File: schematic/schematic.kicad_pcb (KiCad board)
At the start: 4 copper layers, 100 x 100 mm, 260 parts, among them J1 Conn_01x04, J10 Conn_01x03, J11 Conn_01x02, J12 Conn_01x02, J13 Conn_01x02, J14 Conn_01x02, J15 Conn_01x02, J16 Conn_01x02, J17 Conn_01x04, J18 Conn_02x13_Odd_Even, J2 Conn_01x04, J3 Conn_01x04, J4 Conn_01x04, J5 Conn_01x04, J6 Conn_01x06, J7 Conn_01x03, J8 Screw_Terminal_01x02, J9 Conn_01x03, Q1 PSMN1R7-30YL, Q2 PSMN1R7-30YL, Q3 NCV8402, Q4 NCV8402, SW1 SW_Push_Dual, SW2 SW_DIP_x03, U1 STM32F401VETx, U2 TMC2130, U3 TMC2130, U4 TMC2130, U5 TMC2130, U6 BD9E302EFJ, U7 BD9E302EFJ, U8 BD9E302EFJ, Y1 Crystal_GND24

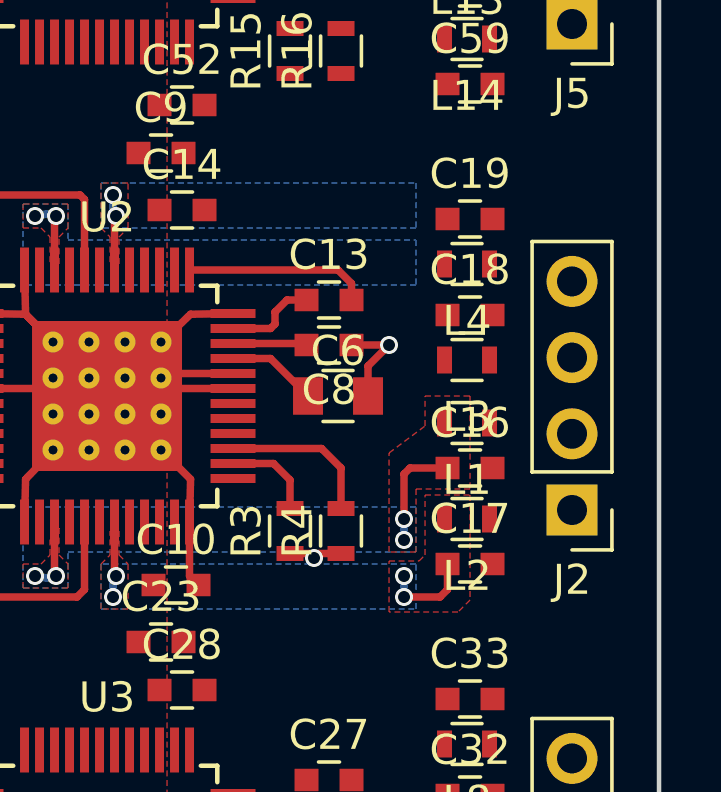
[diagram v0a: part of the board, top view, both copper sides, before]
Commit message: Power layout single driver done
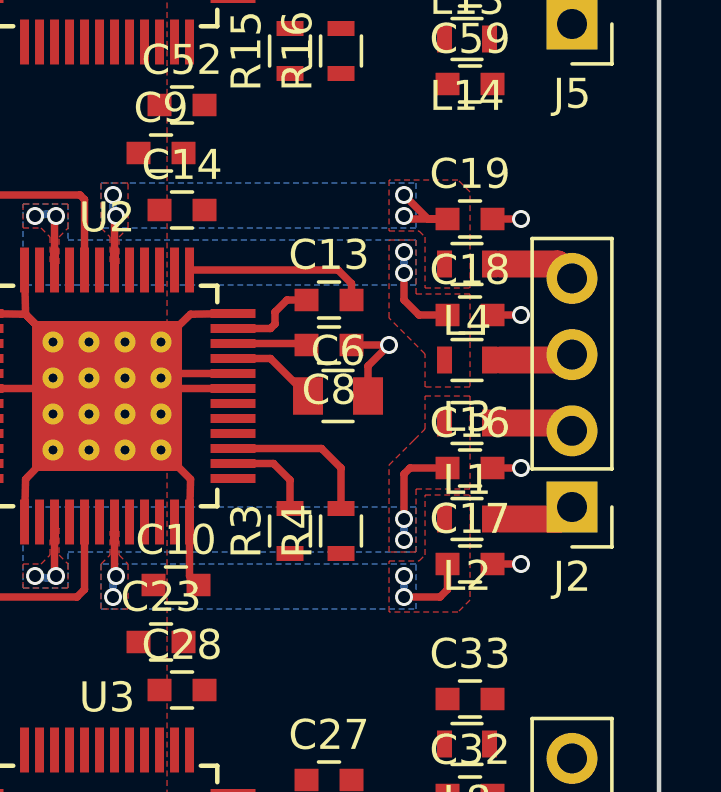
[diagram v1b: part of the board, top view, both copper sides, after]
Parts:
- moved J2 0.10 mm to (262.1, 110.9)
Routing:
- net GND: track 214.8 -> 218.6 mm, vias 78 -> 82
- net Net-(C19-Pad1): track 2.56 -> 5.83 mm, vias 2 -> 4
- net Net-(C18-Pad1): track 2.57 -> 5.83 mm, vias 2 -> 4
- net /MotorX/B2: track 0.00 -> 2.95 mm
- net /MotorX/B1: track 0.00 -> 2.92 mm
- net /MotorX/A1: track 0.00 -> 2.86 mm
- net /MotorX/A2: track 0.00 -> 2.82 mm
- net +3V3: track 3.84 -> 2.01 mm, vias 1 -> 0
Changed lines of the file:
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@@
   (general
     (links 833)
-    (no_connects 352)
+    (no_connects 341)
     (area 133.3 48.325 267.04762 154.782382)
     (thickness 1.6)
     (drawings 4)
-    (tracks 511)
+    (tracks 538)
     (zones 0)
     (modules 260)
@@
     (last_trace_width 0.25)
     (user_trace_width 0.7)
+    (user_trace_width 0.9)
     (user_trace_width 1.5)
     (user_trace_width 2.2)
@@
   )
   (module Socket_Strips:Socket_Strip_Straight_1x04_Pitch2.54mm (layer F.Cu)
-    (at 262.1 111 180)
+    (at 262.1 110.9 180)
     (descr "Through hole straight socket strip, 1x04, 2.54mm pitch, single row")
     (tags "Through hole socket strip THT 1x04 2.54mm single row")
@@
   (gr_line (start 265 50) (end 165 50) (angle 90) (layer Edge.Cuts) (width 0.15))
   (gr_line (start 265 150) (end 265 50) (angle 90) (layer Edge.Cuts) (width 0.15))
+  (segment (start 259.45 101.3) (end 260.4 101.3) (width 0.25) (layer F.Cu) (net 1))
+  (via (at 260.4 101.3) (size 0.6) (drill 0.4) (layers F.Cu B.Cu) (net 1))
+  (segment (start 259.45 104.5) (end 260.4 104.5) (width 0.25) (layer F.Cu) (net 1))
+  (via (at 260.4 104.5) (size 0.6) (drill 0.4) (layers F.Cu B.Cu) (net 1))
+  (segment (start 259.45 112.8) (end 260.4 112.8) (width 0.25) (layer F.Cu) (net 1))
+  (via (at 260.4 112.8) (size 0.6) (drill 0.4) (layers F.Cu B.Cu) (net 1))
+  (segment (start 259.45 109.6) (end 260.4 109.6) (width 0.25) (layer F.Cu) (net 1))
+  (via (at 260.4 109.6) (size 0.6) (drill 0.4) (layers F.Cu B.Cu) (net 1))
   (segment (start 227.3 141.35) (end 227.3 140.6) (width 0.25) (layer B.Cu) (net 1))
   (segment (start 227.3 140.6) (end 228 139.9) (width 0.25) (layer B.Cu) (net 1))
@@
   (segment (start 250.8 105.95) (end 252.05 105.95) (width 0.25) (layer F.Cu) (net 7) (status 10))
   (segment (start 252.05 105.95) (end 253.3 107.2) (width 0.25) (layer F.Cu) (net 7))
-  (segment (start 252.7 112.45) (end 253.35 112.45) (width 0.25) (layer F.Cu) (net 8))
-  (segment (start 253.65 112.45) (end 253.5 112.6) (width 0.25) (layer F.Cu) (net 8))
-  (via (at 253.5 112.6) (size 0.6) (drill 0.4) (layers F.Cu B.Cu) (net 8))
-  (segment (start 253.65 112.45) (end 254.4 112.45) (width 0.25) (layer F.Cu) (net 8))
-  (segment (start 253.35 112.45) (end 253.5 112.6) (width 0.25) (layer F.Cu) (net 8))
   (segment (start 242.4 108.95) (end 240.6 108.95) (width 0.25) (layer F.Cu) (net 8) (status 10))
   (segment (start 240.6 108.95) (end 240.45 109.1) (width 0.25) (layer F.Cu) (net 8))
@@
   (via (at 246.9 113.2) (size 0.6) (drill 0.4) (layers F.Cu B.Cu) (net 16))
   (segment (start 246.85 113.15) (end 246.9 113.2) (width 0.25) (layer F.Cu) (net 16))
+  (segment (start 256.5 102.4) (end 256.5 103.1) (width 0.25) (layer B.Cu) (net 17))
+  (segment (start 257 104.5) (end 256.5 104) (width 0.25) (layer F.Cu) (net 17))
+  (segment (start 256.5 104) (end 256.5 103.1) (width 0.25) (layer F.Cu) (net 17))
+  (via (at 256.5 103.1) (size 0.6) (drill 0.4) (layers F.Cu B.Cu) (net 17))
+  (segment (start 257 104.5) (end 257.95 104.5) (width 0.25) (layer F.Cu) (net 17))
+  (via (at 256.5 102.4) (size 0.6) (drill 0.4) (layers F.Cu B.Cu) (net 17))
   (segment (start 244.85 103) (end 244.85 101.25) (width 0.25) (layer F.Cu) (net 17) (status 10))
   (via (at 244.2 101.2) (size 0.6) (drill 0.4) (layers F.Cu B.Cu) (net 17))
@@
   (via (at 244.9 101.2) (size 0.6) (drill 0.4) (layers F.Cu B.Cu) (net 17))
   (segment (start 244.85 101.25) (end 244.9 101.2) (width 0.25) (layer F.Cu) (net 17))
+  (segment (start 257.95 101.3) (end 256.6 101.3) (width 0.25) (layer F.Cu) (net 18))
+  (via (at 256.5 101.2) (size 0.6) (drill 0.4) (layers F.Cu B.Cu) (net 18))
+  (segment (start 256.6 101.3) (end 256.5 101.2) (width 0.25) (layer F.Cu) (net 18))
+  (segment (start 257.95 101.3) (end 257.3 101.3) (width 0.25) (layer F.Cu) (net 18))
+  (via (at 256.5 100.5) (size 0.6) (drill 0.4) (layers F.Cu B.Cu) (net 18))
+  (segment (start 257.3 101.3) (end 256.5 100.5) (width 0.25) (layer F.Cu) (net 18))
   (segment (start 246.85 103) (end 246.85 101.25) (width 0.25) (layer F.Cu) (net 18) (status 10))
   (via (at 246.8 100.5) (size 0.6) (drill 0.4) (layers F.Cu B.Cu) (net 18))
@@
   (segment (start 215.95 53.67) (end 218.37 53.67) (width 0.7) (layer F.Cu) (net 102))
   (segment (start 218.37 53.67) (end 218.45 53.75) (width 0.7) (layer F.Cu) (net 102))
+  (segment (start 261.92 106) (end 259.7 106) (width 0.9) (layer F.Cu) (net 107) (status 10))
+  (segment (start 259.7 106) (end 259.35 106) (width 0.25) (layer F.Cu) (net 107))
+  (segment (start 261.92 106) (end 262.1 105.82) (width 0.9) (layer F.Cu) (net 107) (status 30))
+  (segment (start 261.84 108.1) (end 259.7 108.1) (width 0.9) (layer F.Cu) (net 108) (status 10))
+  (segment (start 259.7 108.1) (end 259.35 108.1) (width 0.25) (layer F.Cu) (net 108))
+  (segment (start 261.84 108.1) (end 262.1 108.36) (width 0.9) (layer F.Cu) (net 108) (status 30))
+  (segment (start 261.62 102.8) (end 259.7 102.8) (width 0.9) (layer F.Cu) (net 109))
+  (segment (start 259.7 102.8) (end 259.35 102.8) (width 0.25) (layer F.Cu) (net 109))
+  (segment (start 261.62 102.8) (end 262.1 103.28) (width 0.9) (layer F.Cu) (net 109))
+  (segment (start 261.7 111.3) (end 262.1 110.9) (width 0.9) (layer F.Cu) (net 110))
+  (segment (start 261.7 111.3) (end 259.7 111.3) (width 0.9) (layer F.Cu) (net 110))
+  (segment (start 259.7 111.3) (end 259.35 111.3) (width 0.25) (layer F.Cu) (net 110))
   (segment (start 210.675 81.335) (end 210.675 79.675) (width 0.25) (layer F.Cu) (net 119))
   (segment (start 210.675 79.675) (end 210.725 79.625) (width 0.25) (layer F.Cu) (net 119))
@@
     (polygon
       (pts
-        (xy 256.9 112.4) (xy 256 112.4) (xy 256 109.1) (xy 257.2 108.2) (xy 257.2 107.2)
-        (xy 258.5 107.2) (xy 258.7 107.2) (xy 258.7 110.3) (xy 256.9 110.3)
+        (xy 256.9 112.4) (xy 256 112.4) (xy 256 109.5) (xy 256.8 108.7) (xy 256.85 108.65)
+        (xy 257.2 108.3) (xy 257.2 107.2) (xy 258.5 107.2) (xy 258.7 107.2) (xy 258.7 110.3)
+        (xy 256.9 110.3)
       )
     )
@@
       )
     )
+  )
+  (zone (net 18) (net_name "Net-(C19-Pad1)") (layer F.Cu) (hatch edge 0.508)
+    (priority 1)
+    (connect_pads (clearance 0.2))
+    (min_thickness 0.2)
+    (fill yes (arc_segments 16) (thermal_gap 0.1) (thermal_bridge_width 0.3))
+    (polygon
+      (pts
+        (xy 258.7 103.6) (xy 258.7 100.4) (xy 258.3 100) (xy 256 100) (xy 256 101.7)
+        (xy 257 101.7) (xy 257.2 101.9) (xy 257.2 103.6)
+      )
+    )
+  )
+  (zone (net 17) (net_name "Net-(C18-Pad1)") (layer F.Cu) (hatch edge 0.508)
+    (priority 1)
+    (connect_pads (clearance 0.2))
+    (min_thickness 0.2)
+    (fill yes (arc_segments 16) (thermal_gap 0.1) (thermal_bridge_width 0.3))
+    (polygon
+      (pts
+        (xy 256.9 103.8) (xy 258.7 103.8) (xy 258.7 106.9) (xy 257.2 106.9) (xy 257.2 105.8)
+        (xy 256 104.6) (xy 256 102) (xy 256.9 102)
+      )
+    )

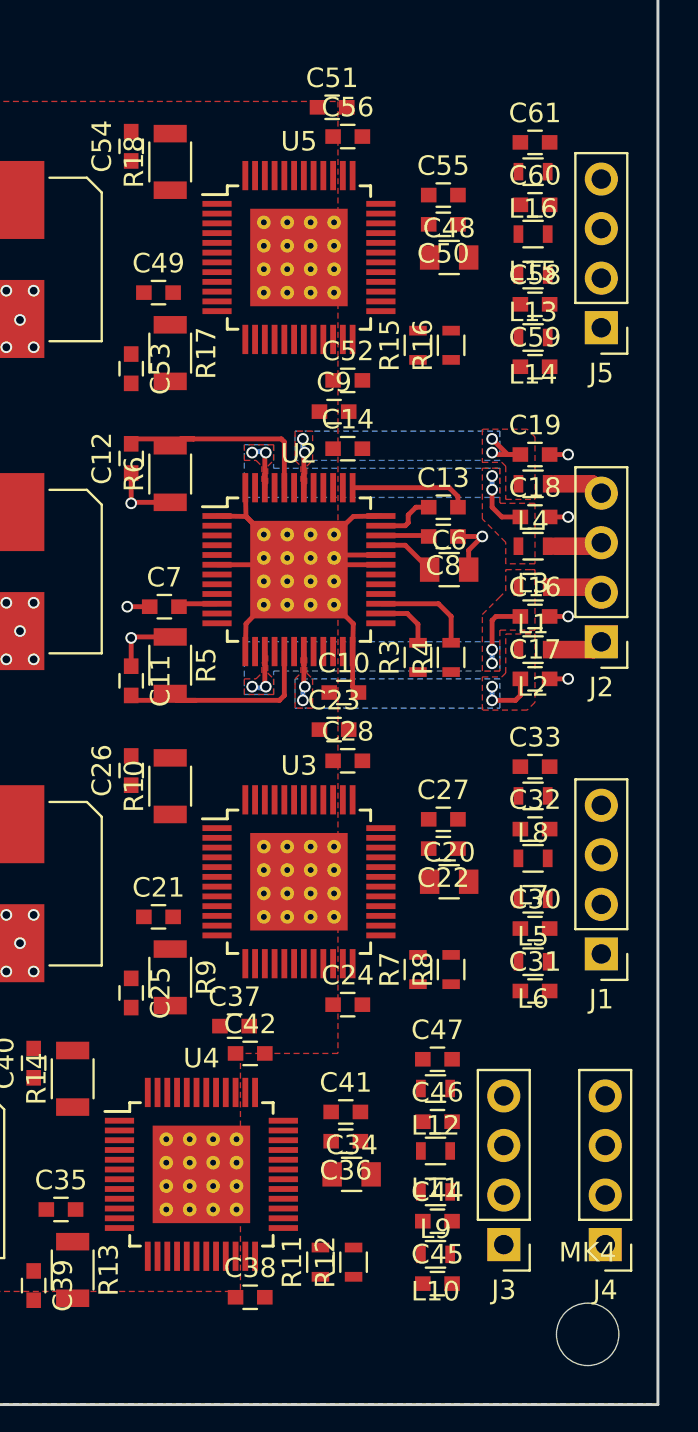
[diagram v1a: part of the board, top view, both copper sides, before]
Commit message: Most power routed to drivers
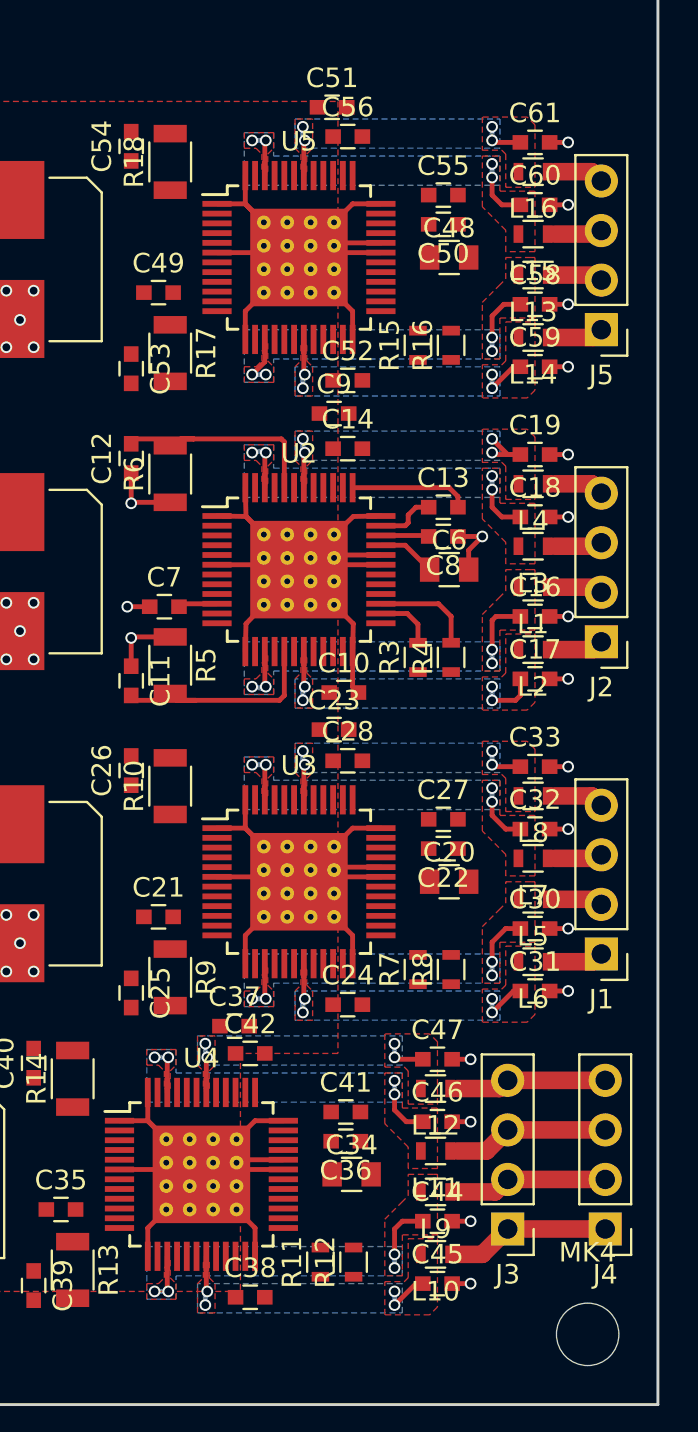
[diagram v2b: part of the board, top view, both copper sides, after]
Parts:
- moved J3 0.82 mm to (257.3, 141.0)
- moved J4 0.80 mm to (262.3, 141.0)
- moved C9 0.10 mm to (248.4, 99.2)
- moved J5 0.10 mm to (262.1, 94.9)
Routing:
- net GND: track 218.6 -> 313.3 mm, vias 82 -> 94
- net /MotorZ/B1: track 0.00 -> 8.49 mm
- net /MotorZ/A2: track 0.00 -> 8.40 mm
- net /MotorZ/B2: track 0.00 -> 8.22 mm
- net /MotorZ/A1: track 0.00 -> 8.22 mm
- net Net-(C58-Pad1): track 0.00 -> 6.27 mm, vias 0 -> 4
- net Net-(C44-Pad1): track 0.00 -> 6.14 mm, vias 0 -> 4
- net Net-(C30-Pad1): track 0.00 -> 5.96 mm, vias 0 -> 4
- net Net-(C60-Pad1): track 0.00 -> 5.78 mm, vias 0 -> 4
- net Net-(C46-Pad1): track 0.00 -> 5.72 mm, vias 0 -> 4
- net Net-(C32-Pad1): track 0.00 -> 5.66 mm, vias 0 -> 4
- net Net-(C45-Pad1): track 0.00 -> 5.17 mm, vias 0 -> 4
- net Net-(C59-Pad1): track 0.00 -> 5.17 mm, vias 0 -> 4
- net Net-(C31-Pad1): track 0.00 -> 5.17 mm, vias 0 -> 4
- net Net-(C47-Pad1): track 0.00 -> 4.75 mm, vias 0 -> 4
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- added copper zone on B.Cu, net Net-(C30-Pad1)
- added copper zone on F.Cu, net Net-(C30-Pad1)
- added copper zone on B.Cu, net Net-(C31-Pad1)
- added copper zone on F.Cu, net Net-(C31-Pad1)
- added copper zone on B.Cu, net Net-(C32-Pad1)
- added copper zone on F.Cu, net Net-(C32-Pad1)
- added copper zone on B.Cu, net Net-(C33-Pad1)
- added copper zone on F.Cu, net Net-(C33-Pad1)
- added copper zone on B.Cu, net Net-(C44-Pad1)
- added copper zone on F.Cu, net Net-(C44-Pad1)
- added copper zone on B.Cu, net Net-(C45-Pad1)
- added copper zone on F.Cu, net Net-(C45-Pad1)
- added copper zone on B.Cu, net Net-(C46-Pad1)
- added copper zone on F.Cu, net Net-(C46-Pad1)
- added copper zone on B.Cu, net Net-(C47-Pad1)
- added copper zone on F.Cu, net Net-(C47-Pad1)
- added copper zone on B.Cu, net Net-(C58-Pad1)
- added copper zone on F.Cu, net Net-(C58-Pad1)
- added copper zone on B.Cu, net Net-(C59-Pad1)
- added copper zone on F.Cu, net Net-(C59-Pad1)
- added copper zone on B.Cu, net Net-(C60-Pad1)
- added copper zone on F.Cu, net Net-(C60-Pad1)
- added copper zone on B.Cu, net Net-(C61-Pad1)
- added copper zone on F.Cu, net Net-(C61-Pad1)

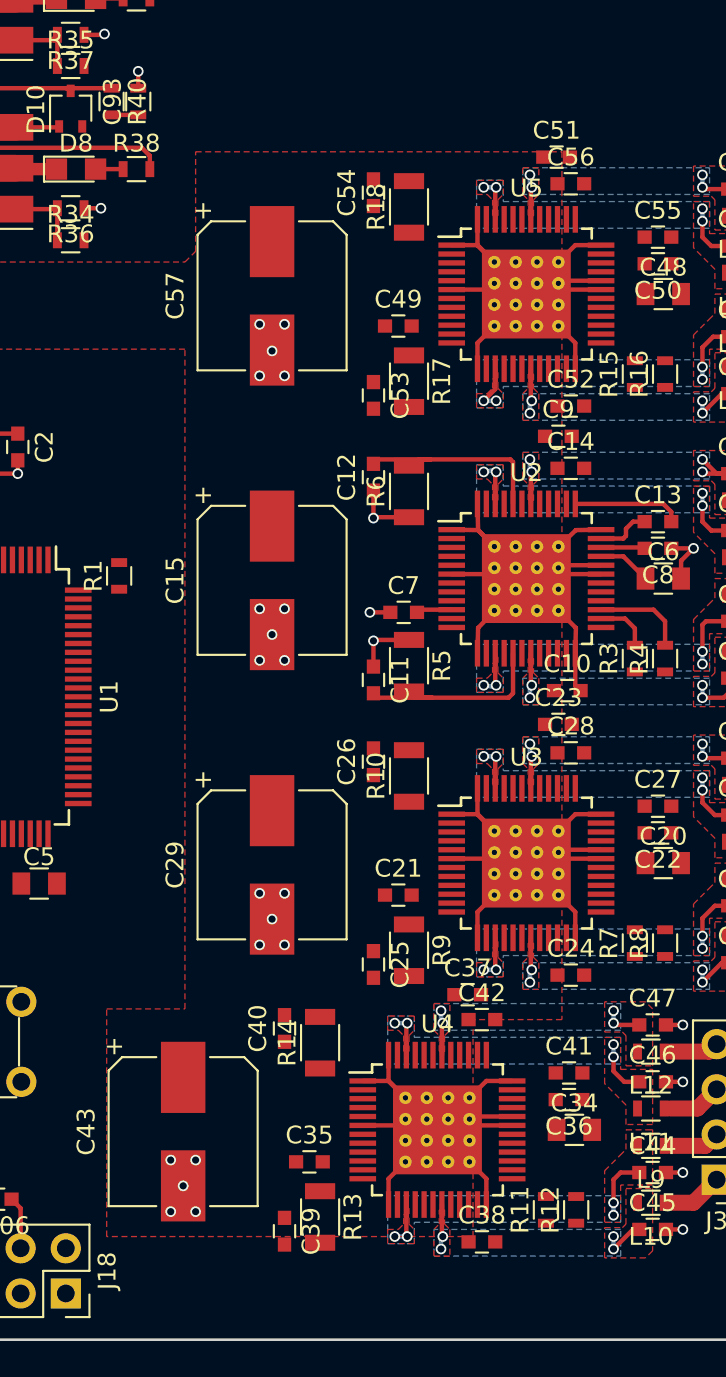
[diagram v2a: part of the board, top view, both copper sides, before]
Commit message: Moved capacitors for better power connection
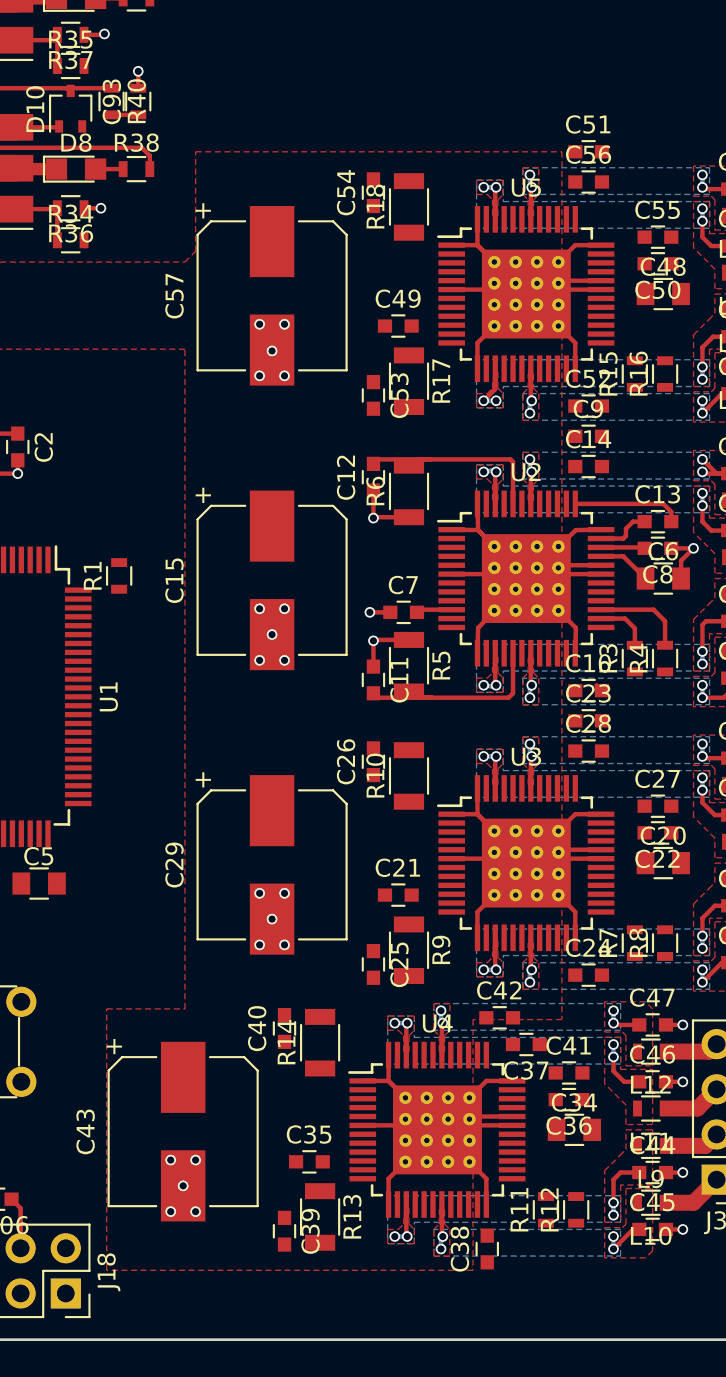
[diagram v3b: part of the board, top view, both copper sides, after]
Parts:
- moved C37 4.33 mm to (246.6, 133.4), turned to 180 degrees
- moved C51 1.82 mm to (250.1, 83.2)
- moved C23 1.71 mm to (250.1, 115.2)
- moved C9 1.70 mm to (250.1, 99.2)
- moved C10 1.20 mm to (250.1, 113.5)
- moved C14 1.00 mm to (250.1, 100.9)
- moved C28 1.00 mm to (250.1, 116.9)
- moved C42 1.00 mm to (245.1, 131.9)
- moved C56 1.00 mm to (250.1, 84.9)
- moved C24 1.00 mm to (250.1, 129.5)
- moved C52 1.00 mm to (250.1, 97.5)
- moved C38 0.50 mm to (244.4, 144.9), turned to 90 degrees
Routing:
- net GND: track 313.3 -> 311.5 mm

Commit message: More driver routing
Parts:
- moved C42 3.89 mm to (248.6, 133.6), turned to 270 degrees
- moved C27 3.00 mm to (251.3, 118.7), turned to 180 degrees
- moved C41 2.91 mm to (246.4, 133.7), turned to 180 degrees
- moved C13 2.91 mm to (251.4, 102.7), turned to 180 degrees
- moved C55 2.91 mm to (251.4, 86.7), turned to 180 degrees
- moved C37 1.12 mm to (246.4, 132.3)
- moved C24 0.81 mm to (249.4, 129.9), turned to 90 degrees
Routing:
- net GND: track 311.5 -> 362.7 mm, vias 94 -> 110
- net +12C: track 0.00 -> 15.1 mm
- net Net-(C26-Pad2): track 0.00 -> 11.9 mm
- net Net-(C53-Pad2): track 0.00 -> 11.9 mm
- net Net-(C40-Pad2): track 0.00 -> 11.8 mm
- net Net-(C39-Pad2): track 0.00 -> 11.8 mm
- net Net-(C25-Pad2): track 0.00 -> 11.8 mm
- net Net-(C54-Pad2): track 0.00 -> 11.6 mm
- net +5V: track 5.44 -> 12.9 mm
- net Net-(C51-Pad2): track 0.00 -> 5.42 mm
- net Net-(C9-Pad2): track 0.00 -> 5.42 mm
- net Net-(C23-Pad2): track 0.00 -> 5.18 mm
- net Net-(C13-Pad2): track 6.14 -> 1.42 mm
- net Net-(C41-Pad1): track 0.00 -> 3.48 mm
- net Net-(C55-Pad1): track 0.00 -> 3.48 mm
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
